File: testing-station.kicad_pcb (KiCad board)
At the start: 2 copper layers, 0 parts

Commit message: switched to 4 layer board
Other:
- copper layers 2 -> 4
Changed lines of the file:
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@@
 	(layers
 		(0 "F.Cu" signal)
+		(1 "In1.Cu" signal)
+		(2 "In2.Cu" signal)
 		(31 "B.Cu" signal)
 		(32 "B.Adhes" user "B.Adhesive")
@@
 			)
 			(layer "dielectric 1"
+				(type "prepreg")
+				(color "FR4 natural")
+				(thickness 0.1)
+				(material "FR4")
+				(epsilon_r 4.5)
+				(loss_tangent 0.02)
+			)
+			(layer "In1.Cu"
+				(type "copper")
+				(thickness 0.035)
+			)
+			(layer "dielectric 2"
 				(type "core")
 				(color "FR4 natural")
-				(thickness 1.51)
+				(thickness 1.24)
 				(material "FR4")
 				(epsilon_r 4.5)
+				(loss_tangent 0.02)
+			)
+			(layer "In2.Cu"
+				(type "copper")
+				(thickness 0.035)
+			)
+			(layer "dielectric 3"
+				(type "prepreg")
+				(color "FR4 natural")
+				(thickness 0.1)
+				(material "FR4")
+				(epsilon_r 4.5)

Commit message: added Arduino UNO R4 in root sheet
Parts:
- added A1: Arduino_Uno_R4_WiFi_Shield, PCM_arduino-library:Arduino_Uno_R4_WiFi_Shield, B.Cu at (238.6, 123.8)

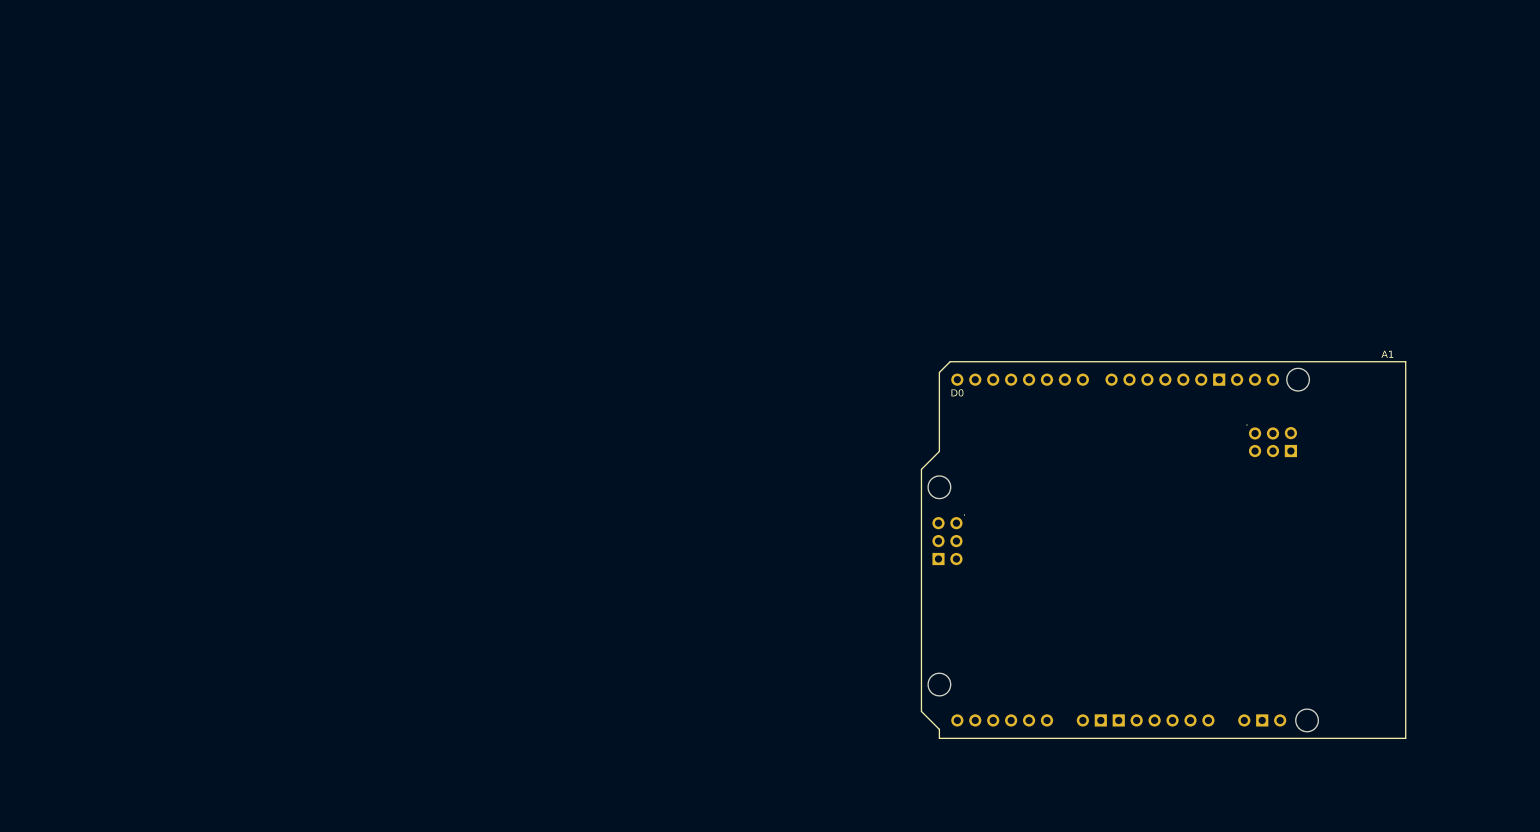
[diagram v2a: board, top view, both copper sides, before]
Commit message: added pyrano, anemo, AM2315C, power supply, LEDs, switch and FPC connector in schematic
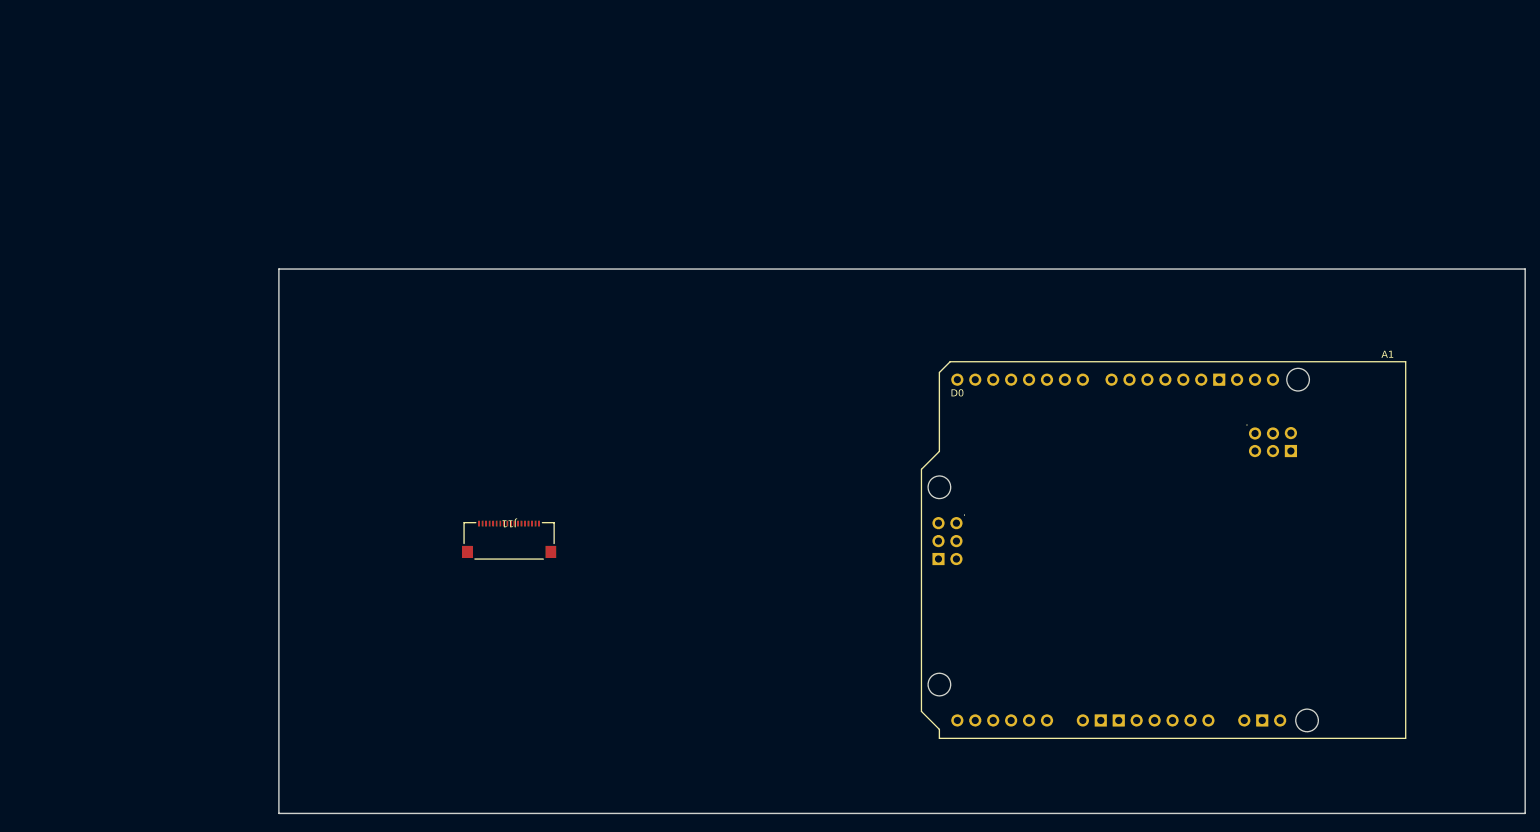
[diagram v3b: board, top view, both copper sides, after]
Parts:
- added J11: FPC connector, external_footprints:XF2M-1815-1A, F.Cu at (111.6, 95.8)
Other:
- board outline added: 176.5 x 77.1 mm

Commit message: removed connectors from modules
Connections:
- A1 pad A0: unconnected-(A1-PadA0) -> /A0
- A1 pad A5: unconnected-(A1-PadA5) -> /A5
- A1 pad D11: unconnected-(A1-PadD11) -> /MOSI
- A1 pad D12: unconnected-(A1-PadD12) -> /MISO
- A1 pad D13: unconnected-(A1-PadD13) -> /SCK
- A1 pad D2: unconnected-(A1-PadD2) -> /D2
- A1 pad D3: unconnected-(A1-PadD3) -> /D3
- A1 pad D5: unconnected-(A1-PadD5) -> /D5
- A1 pad D7: unconnected-(A1-PadD7) -> /D7
- A1 pad D8: unconnected-(A1-PadD8) -> /D8
- A1 pad D9: unconnected-(A1-PadD9) -> /D9
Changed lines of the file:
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@@
 	)
 	(net 0 "")
-	(net 1 "unconnected-(A1-PadD11)")
+	(net 1 "/MOSI")
 	(net 2 "unconnected-(A1-D1{slash}TX-PadD1)")
 	(net 3 "unconnected-(A1-GND-PadGND3)")
-	(net 4 "unconnected-(A1-PadD5)")
+	(net 4 "/D5")
 	(net 5 "/D4")
 	(net 6 "unconnected-(A1-PadVIN)")
-	(net 7 "unconnected-(A1-PadD7)")
+	(net 7 "/D7")
 	(net 8 "unconnected-(A1-IOREF-PadIORF)")
-	(net 9 "unconnected-(A1-PadD9)")
+	(net 9 "/D9")
 	(net 10 "unconnected-(A1-PadD10)")
 	(net 11 "/SCA")
 	(net 12 "unconnected-(A1-GND-PadGND2)")
-	(net 13 "unconnected-(A1-PadD3)")
+	(net 13 "/D3")
 	(net 14 "unconnected-(A1-RESET-PadRST1)")
 	(net 15 "unconnected-(A1-SPI_SCK-PadSCK)")
-	(net 16 "unconnected-(A1-PadA0)")
+	(net 16 "/A0")
 	(net 17 "/A1")
-	(net 18 "unconnected-(A1-PadD12)")
+	(net 18 "/MISO")
 	(net 19 "unconnected-(A1-VRTC-PadVBAT)")
 	(net 20 "unconnected-(A1-D0{slash}RX-PadD0)")
 	(net 21 "unconnected-(A1-GND-PadGND1)")
-	(net 22 "unconnected-(A1-PadD2)")
+	(net 22 "/D2")
 	(net 23 "unconnected-(A1-PadAREF)")
 	(net 24 "unconnected-(A1-ESP_RX-PadESP5)")
@@
 	(net 26 "unconnected-(A1-GND-PadGND5)")
 	(net 27 "unconnected-(A1-GND-PadGND4)")
-	(net 28 "unconnected-(A1-PadA5)")
+	(net 28 "/A5")
 	(net 29 "unconnected-(A1-GND-PadGND4)_0")
 	(net 30 "unconnected-(A1-SPI_5V-Pad5V2)")
@@
 	(net 35 "unconnected-(A1-SPI_RESET-PadRST2)")
 	(net 36 "unconnected-(A1-SPI_MISO-PadMISO)")
-	(net 37 "unconnected-(A1-PadD8)")
+	(net 37 "/D8")
 	(net 38 "/A3")
 	(net 39 "/SCL")
@@
 	(net 44 "/D6")
 	(net 45 "/A2")
-	(net 46 "unconnected-(A1-PadD13)")
+	(net 46 "/SCK")
 	(net 47 "unconnected-(A1-ESP_42-PadESP1)")
 	(net 48 "unconnected-(J11-Pin_3-Pad3)")
@@
 			(layers "*.Cu" "*.Mask")
 			(remove_unused_layers no)
-			(net 16 "unconnected-(A1-PadA0)")
+			(net 16 "/A0")
 			(pinfunction "A0")
-			(pintype "bidirectional+no_connect")
+			(pintype "bidirectional")
 		)
 		(pad "A1" thru_hole oval
@@
 			(layers "*.Cu" "*.Mask")
 			(remove_unused_layers no)
-			(net 28 "unconnected-(A1-PadA5)")
+			(net 28 "/A5")
 			(pinfunction "A5")
-			(pintype "bidirectional+no_connect")
+			(pintype "bidirectional")
 		)
 		(pad "AREF" thru_hole oval
@@
 			(layers "*.Cu" "*.Mask")
 			(remove_unused_layers no)
-			(net 22 "unconnected-(A1-PadD2)")
+			(net 22 "/D2")
 			(pinfunction "D2")
-			(pintype "bidirectional+no_connect")
+			(pintype "bidirectional")
 		)
 		(pad "D3" thru_hole oval
@@
 			(layers "*.Cu" "*.Mask")
 			(remove_unused_layers no)
-			(net 13 "unconnected-(A1-PadD3)")
+			(net 13 "/D3")
 			(pinfunction "D3")
-			(pintype "bidirectional+no_connect")
+			(pintype "bidirectional")
 		)
 		(pad "D4" thru_hole oval
@@
 			(layers "*.Cu" "*.Mask")
 			(remove_unused_layers no)
-			(net 4 "unconnected-(A1-PadD5)")
+			(net 4 "/D5")
 			(pinfunction "D5")
-			(pintype "bidirectional+no_connect")
+			(pintype "bidirectional")
 		)
 		(pad "D6" thru_hole oval
@@
 			(layers "*.Cu" "*.Mask")
 			(remove_unused_layers no)
-			(net 7 "unconnected-(A1-PadD7)")
+			(net 7 "/D7")
 			(pinfunction "D7")
-			(pintype "bidirectional+no_connect")
+			(pintype "bidirectional")
 		)
 		(pad "D8" thru_hole oval
@@
 			(layers "*.Cu" "*.Mask")
 			(remove_unused_layers no)
-			(net 37 "unconnected-(A1-PadD8)")
+			(net 37 "/D8")
 			(pinfunction "D8")
-			(pintype "bidirectional+no_connect")
+			(pintype "bidirectional")
 		)
 		(pad "D9" thru_hole oval
@@
 			(layers "*.Cu" "*.Mask")
 			(remove_unused_layers no)
-			(net 9 "unconnected-(A1-PadD9)")
+			(net 9 "/D9")
 			(pinfunction "D9")
-			(pintype "bidirectional+no_connect")
+			(pintype "bidirectional")
 		)
 		(pad "D10" thru_hole oval
@@
 			(layers "*.Cu" "*.Mask")
 			(remove_unused_layers no)
-			(net 1 "unconnected-(A1-PadD11)")
+			(net 1 "/MOSI")
 			(pinfunction "D11")
-			(pintype "bidirectional+no_connect")
+			(pintype "bidirectional")
 		)
 		(pad "D12" thru_hole oval
@@
 			(layers "*.Cu" "*.Mask")
 			(remove_unused_layers no)
-			(net 18 "unconnected-(A1-PadD12)")
+			(net 18 "/MISO")
 			(pinfunction "D12")
-			(pintype "bidirectional+no_connect")
+			(pintype "bidirectional")
 		)
 		(pad "D13" thru_hole oval
@@
 			(layers "*.Cu" "*.Mask")
 			(remove_unused_layers no)
-			(net 46 "unconnected-(A1-PadD13)")
+			(net 46 "/SCK")
 			(pinfunction "D13")
-			(pintype "bidirectional+no_connect")
+			(pintype "bidirectional")
 		)
 		(pad "ESP1" thru_hole oval

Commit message: added PCB layout
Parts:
- removed J11: FPC connector, external_footprints:XF2M-1815-1A
- added B1: CR1220, external_footprints:CR1220, F.Cu at (116.7, 88.1)
- added C1: 0.1uF, Capacitor_SMD:C_0805_2012Metric, F.Cu at (74.5, 35.5)
- added C10: 10uF, Capacitor_SMD:C_0805_2012Metric, F.Cu at (111.8, 49.7)
- added C11: 0.1uF, Capacitor_SMD:C_0805_2012Metric, F.Cu at (145.8, 38.4)
- added C12: 0.1uF, Capacitor_SMD:C_0805_2012Metric, F.Cu at (145.8, 41.4)
- added C13: 0.1uF, Capacitor_SMD:C_0805_2012Metric, F.Cu at (145.8, 44.5)
- added C14: 10uF, Capacitor_SMD:C_0805_2012Metric, F.Cu at (145.8, 47.5)
- added C15: 10uF, Capacitor_SMD:C_0805_2012Metric, F.Cu at (145.8, 50.5)
- added C16: 10uF, Capacitor_SMD:C_0805_2012Metric, F.Cu at (80.4, 78.5)
- added C17: 0.1uF, Capacitor_SMD:C_0603_1608Metric, F.Cu at (76.2, 65.1)
- added C18: 10uF, Capacitor_SMD:C_0805_2012Metric, F.Cu at (80.4, 81.5)
- added C19: 1uF, Capacitor_SMD:C_0805_2012Metric, F.Cu at (118.8, 64.6)
- added C2: 0.1uF, Capacitor_SMD:C_0805_2012Metric, F.Cu at (74.5, 38.5)
- added C20: 10uF, Capacitor_SMD:C_0805_2012Metric, F.Cu at (166.6, 77.9)
- added C21: 0.1uF, Capacitor_SMD:C_0805_2012Metric, F.Cu at (166.6, 80.9)
- added C3: 0.1uF, Capacitor_SMD:C_0805_2012Metric, F.Cu at (74.5, 41.5)
- added C4: 10uF, Capacitor_SMD:C_0805_2012Metric, F.Cu at (74.5, 44.5)
- added C5: 10uF, Capacitor_SMD:C_0805_2012Metric, F.Cu at (74.5, 47.5)
- added C6: 0.1uF, Capacitor_SMD:C_0805_2012Metric, F.Cu at (111.8, 37.6)
- added C7: 0.1uF, Capacitor_SMD:C_0805_2012Metric, F.Cu at (111.8, 40.6)
- added C8: 0.1uF, Capacitor_SMD:C_0805_2012Metric, F.Cu at (111.8, 43.6)
- added C9: 10uF, Capacitor_SMD:C_0805_2012Metric, F.Cu at (111.8, 46.7)
- added D1: LED_GREEN, LED_SMD:LED_1206_3216Metric_Pad1.42x1.75mm_HandSolder, F.Cu at (56.8, 50.1)
- added D10: 1N4148, Diode_SMD:D_SOD-323, F.Cu at (162.5, 32.3)
- added D11: 1N4148, Diode_SMD:D_SOD-323, F.Cu at (162.5, 35.2)
- added D12: GREEN, LED_SMD:LED_0603_1608Metric, F.Cu at (91.0, 81.0)
- added D13: 1N4148, Diode_SMD:D_SOD-323, F.Cu at (86.9, 78.2)
- added D14: RED, LED_SMD:LED_0805_2012Metric, F.Cu at (155.5, 83.6)
- added D2: LED_RED, LED_SMD:LED_1206_3216Metric_Pad1.42x1.75mm_HandSolder, F.Cu at (56.9, 54.1)
- added D3: 1N4148, Diode_SMD:D_SOD-323, F.Cu at (91.2, 26.4)
- added D4: 1N4148, Diode_SMD:D_SOD-323, F.Cu at (91.2, 29.3)
- added D5: 1N4148, Diode_SMD:D_SOD-323, F.Cu at (91.2, 32.3)
- added D6: 1N4148, Diode_SMD:D_SOD-323, F.Cu at (128.5, 28.6)
- added D7: 1N4148, Diode_SMD:D_SOD-323, F.Cu at (128.5, 31.5)
- added D8: 1N4148, Diode_SMD:D_SOD-323, F.Cu at (128.5, 34.5)
- added D9: 1N4148, Diode_SMD:D_SOD-323, F.Cu at (162.5, 29.4)
- added FB1: FERRITE-0805NO, Inductor_SMD:L_0805_2012Metric, F.Cu at (83.5, 45.4)
- added FB2: FERRITE-0805NO, Inductor_SMD:L_0805_2012Metric, F.Cu at (120.7, 47.6)
- added FB3: FERRITE-0805NO, Inductor_SMD:L_0805_2012Metric, F.Cu at (154.8, 48.4)
- added IC1: BME680, Package_LGA:Bosch_LGA-8_3x3mm_P0.8mm_ClockwisePinNumbering, F.Cu at (87.2, 70.9)
- added IC2: DS3231, Package_SO:SOIC-16W_7.5x10.3mm_P1.27mm, F.Cu at (117.7, 74.6)
- added IC3: 74HC4050D, Package_SO:SOIC-16_3.9x9.9mm_P1.27mm, F.Cu at (168.6, 70.7)
- added IC4: LP2985A, Package_TO_SOT_SMD:SOT-23-5, F.Cu at (150.7, 84.5)
- added J1: pyranometer, TerminalBlock:TerminalBlock_bornier-4_P5.08mm, F.Cu at (137.5, 109.4)
- added J13: microSD, external_footprints:MEM2061-01-188-00-A, F.Cu at (156.1, 73.6)
- added J2: anemometer, TerminalBlock:TerminalBlock_bornier-3_P5.08mm, F.Cu at (182.3, 109.6)
- added J3: AM2315C, TerminalBlock:TerminalBlock_bornier-4_P5.08mm, F.Cu at (160.0, 109.5)
- added J4: FPC connector, external_footprints:XF2M-1815-1A, F.Cu at (230.9, 94.1)
- added J5: Pt100, TerminalBlock_4Ucon:TerminalBlock_4Ucon_1x04_P3.50mm_Horizontal, F.Cu at (74.3, 28.3)
- added J7: Pt100, TerminalBlock_4Ucon:TerminalBlock_4Ucon_1x04_P3.50mm_Horizontal, F.Cu at (111.4, 29.0)
- added J9: Pt100, TerminalBlock_4Ucon:TerminalBlock_4Ucon_1x04_P3.50mm_Horizontal, F.Cu at (145.8, 29.4)
- added JP1: SolderJumper_3_Bridged12, Jumper:SolderJumper-3_P1.3mm_Bridged12_Pad1.0x1.5mm, F.Cu at (93.4, 47.6)
- added JP2: SOLDERJUMPER, Jumper:SolderJumper-2_P1.3mm_Open_RoundedPad1.0x1.5mm, F.Cu at (88.4, 43.0)
- added JP3: SOLDERJUMPER, Jumper:SolderJumper-2_P1.3mm_Open_RoundedPad1.0x1.5mm, F.Cu at (88.4, 46.5)
- added JP4: SolderJumper_3_Bridged12, Jumper:SolderJumper-3_P1.3mm_Bridged12_Pad1.0x1.5mm, F.Cu at (130.7, 49.8)
- added JP5: SOLDERJUMPER, Jumper:SolderJumper-2_P1.3mm_Open_RoundedPad1.0x1.5mm, F.Cu at (125.7, 45.1)
- added JP6: SOLDERJUMPER, Jumper:SolderJumper-2_P1.3mm_Open_RoundedPad1.0x1.5mm, F.Cu at (125.7, 48.7)
- added JP7: SolderJumper_3_Bridged12, Jumper:SolderJumper-3_P1.3mm_Bridged12_Pad1.0x1.5mm, F.Cu at (164.7, 50.6)
- added JP8: SOLDERJUMPER, Jumper:SolderJumper-2_P1.3mm_Open_RoundedPad1.0x1.5mm, F.Cu at (159.7, 46.0)
- added JP9: SOLDERJUMPER, Jumper:SolderJumper-2_P1.3mm_Open_RoundedPad1.0x1.5mm, F.Cu at (159.7, 49.5)
- added Q1: BSS138, Package_TO_SOT_SMD:SOT-363_SC-70-6, F.Cu at (86.9, 81.7)
- added R1: 10k, Resistor_SMD:R_1206_3216Metric_Pad1.30x1.75mm_HandSolder, F.Cu at (56.8, 43.1)
- added R10: 10K, Resistor_SMD:R_0805_2012Metric, F.Cu at (116.2, 43.5)
- added R11: 430Ω, ±0.1%, Resistor_SMD:R_0805_2012Metric, F.Cu at (116.2, 46.5)
- added R12: 10K, Resistor_SMD:R_0805_2012Metric, F.Cu at (150.3, 38.4)
- added R13: 10K, Resistor_SMD:R_0805_2012Metric, F.Cu at (150.3, 41.4)
- added R14: 10K, Resistor_SMD:R_0805_2012Metric, F.Cu at (150.3, 44.3)
- added R15: 430Ω, ±0.1%, Resistor_SMD:R_0805_2012Metric, F.Cu at (150.3, 47.2)
- added R16: 10k, Resistor_SMD:R_0603_1608Metric, F.Cu at (76.2, 67.6)
- added R17: 10k, Resistor_SMD:R_0603_1608Metric, F.Cu at (76.2, 70.1)
- added R18: 10k, Resistor_SMD:R_0603_1608Metric, F.Cu at (76.2, 72.6)
- added R19: 10k, Resistor_SMD:R_0603_1608Metric, F.Cu at (76.2, 75.1)
- added R2: 150, Resistor_SMD:R_1206_3216Metric_Pad1.30x1.75mm_HandSolder, F.Cu at (50.3, 50.1)
- added R20: 10k, Resistor_SMD:R_0603_1608Metric, F.Cu at (76.2, 77.7)
- added R21: 10k, Resistor_SMD:R_0603_1608Metric, F.Cu at (76.2, 80.2)
- added R22: 10k, Resistor_SMD:R_0603_1608Metric, F.Cu at (76.2, 82.7)
- added R23: 10k, Resistor_SMD:R_0805_2012Metric, F.Cu at (112.5, 65.1)
- added R24: 10k, Resistor_SMD:R_0805_2012Metric, F.Cu at (124.4, 65.3)
- added R25: 1k, Resistor_SMD:R_0805_2012Metric, F.Cu at (159.9, 83.6)
- added R3: 150, Resistor_SMD:R_1206_3216Metric_Pad1.30x1.75mm_HandSolder, F.Cu at (50.1, 54.3)
- added R4: 10K, Resistor_SMD:R_0805_2012Metric, F.Cu at (79.0, 35.4)
- added R5: 10K, Resistor_SMD:R_0805_2012Metric, F.Cu at (79.0, 38.4)
- added R6: 10K, Resistor_SMD:R_0805_2012Metric, F.Cu at (79.0, 41.3)
- added R7: 430Ω, ±0.1%, Resistor_SMD:R_0805_2012Metric, F.Cu at (79.0, 44.3)
- added R8: 10K, Resistor_SMD:R_0805_2012Metric, F.Cu at (116.2, 37.6)
- added R9: 10K, Resistor_SMD:R_0805_2012Metric, F.Cu at (116.2, 40.5)
- added SJ1: SOLDERJUMPER, Jumper:SolderJumper-2_P1.3mm_Open_TrianglePad1.0x1.5mm, F.Cu at (86.9, 75.0)
- added SW1: 500SSP1S2M2QEA, external_footprints:500SSP1S2M2QEA, F.Cu at (54.2, 36.7)
- added U$1: MOUNTINGHOLE2.5, MountingHole:MountingHole_2.2mm_M2_ISO7380, F.Cu at (83.7, 36.5)
- added U$10: MOUNTINGHOLE2.5, MountingHole:MountingHole_2.5mm, F.Cu at (130.4, 90.7)
- added U$2: MOUNTINGHOLE2.5, MountingHole:MountingHole_2.2mm_M2_ISO7380, F.Cu at (83.7, 41.5)
- added U$3: MOUNTINGHOLE2.5, MountingHole:MountingHole_2.2mm_M2_ISO7380, F.Cu at (121.0, 38.6)
- added U$4: MOUNTINGHOLE2.5, MountingHole:MountingHole_2.2mm_M2_ISO7380, F.Cu at (121.0, 43.7)
- added U$5: MOUNTINGHOLE2.5, MountingHole:MountingHole_2.2mm_M2_ISO7380, F.Cu at (155.0, 39.5)
- added U$6: MOUNTINGHOLE2.5, MountingHole:MountingHole_2.2mm_M2_ISO7380, F.Cu at (155.0, 44.5)
- added U$7: MOUNTINGHOLE2.5, MountingHole:MountingHole_2.5mm, F.Cu at (81.5, 67.1)
- added U$8: MOUNTINGHOLE2.5, MountingHole:MountingHole_2.5mm, F.Cu at (81.5, 73.7)
- added U$9: MOUNTINGHOLE2.5, MountingHole:MountingHole_2.5mm, F.Cu at (130.4, 84.2)
- added U1: TBA_1-0519, external_footprints:TBA_1-0519, F.Cu at (117.8, 108.2)
- added U2: MAX31865, Package_DFN_QFN:TQFN-20-1EP_5x5mm_P0.65mm_EP3.25x3.25mm, F.Cu at (89.8, 37.6)
- added U3: MIC5225, Package_TO_SOT_SMD:SOT-23-5, F.Cu at (93.2, 43.6)
- added U4: MAX31865, Package_DFN_QFN:TQFN-20-1EP_5x5mm_P0.65mm_EP3.25x3.25mm, F.Cu at (127.1, 39.8)
- added U5: MIC5225, Package_TO_SOT_SMD:SOT-23-5, F.Cu at (130.4, 45.8)
- added U6: MAX31865, Package_DFN_QFN:TQFN-20-1EP_5x5mm_P0.65mm_EP3.25x3.25mm, F.Cu at (161.2, 40.5)
- added U7: MIC5225, Package_TO_SOT_SMD:SOT-23-5, F.Cu at (164.4, 46.6)
- added U8: AP2112K-3.3, Package_TO_SOT_SMD:SOT-23-5, F.Cu at (87.3, 66.2)
- moved A1 46.3 mm to (249.7, 78.8)
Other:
- board size 176.5 x 77.1 mm -> 212.7 x 113.3 mm

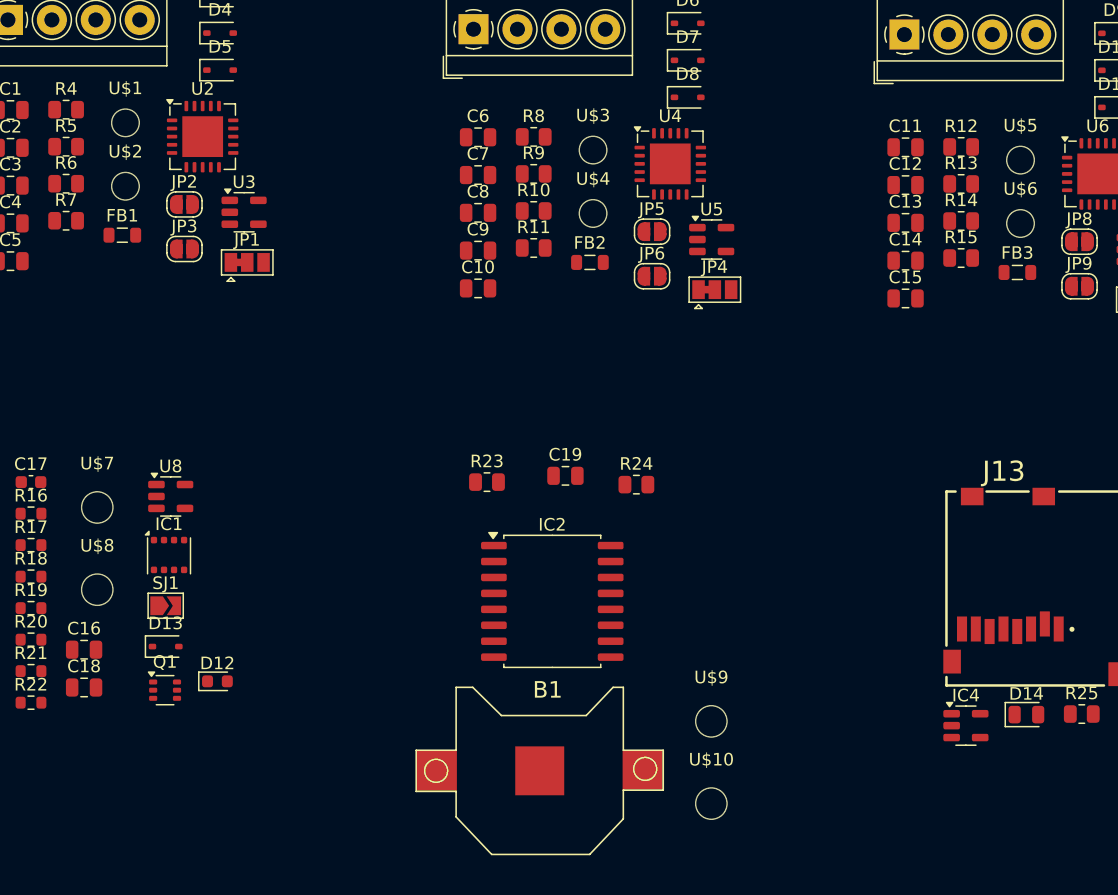
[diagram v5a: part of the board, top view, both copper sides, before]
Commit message: removed mouting holes
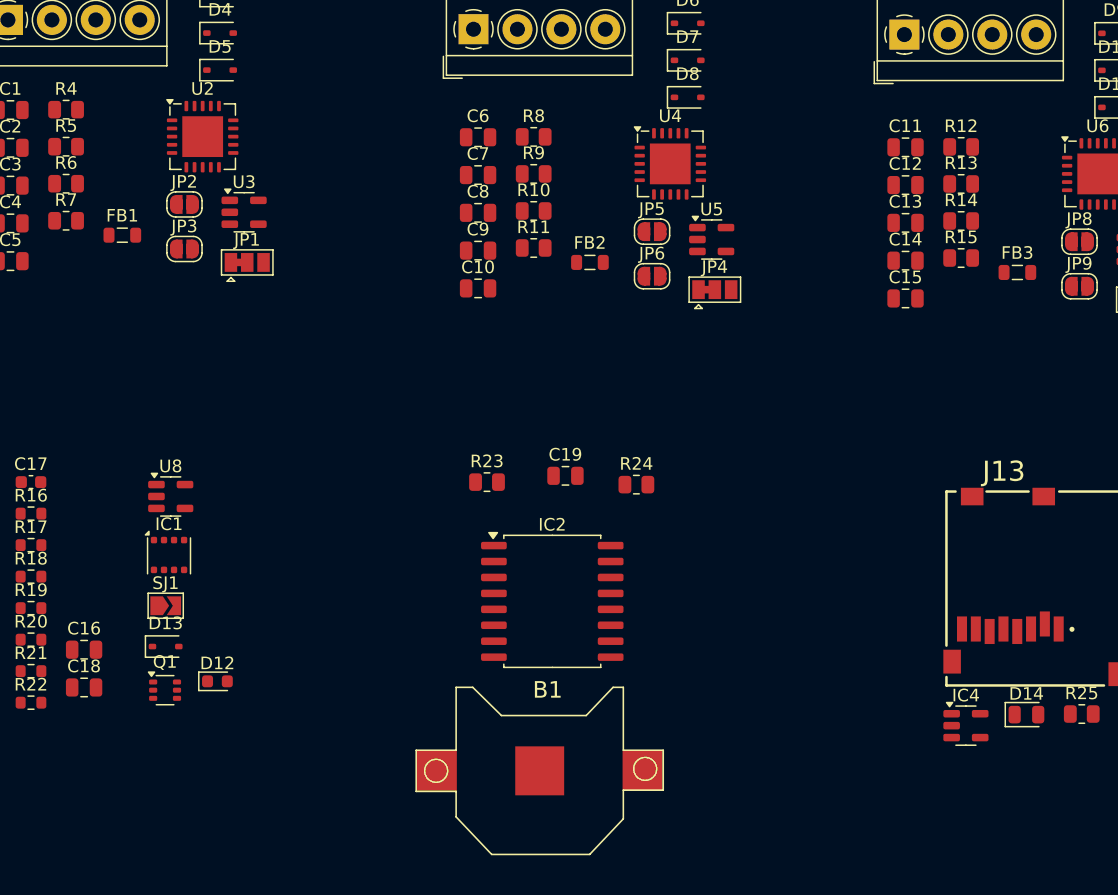
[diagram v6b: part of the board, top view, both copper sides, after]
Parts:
- removed U$1, U$2, U$3, U$4, U$5, U$6: MOUNTINGHOLE2.5, MountingHole:MountingHole_2.2mm_M2_ISO7380
- removed U$10, U$7, U$8, U$9: MOUNTINGHOLE2.5, MountingHole:MountingHole_2.5mm
